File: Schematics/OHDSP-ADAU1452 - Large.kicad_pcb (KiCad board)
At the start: 2 copper layers, 100 x 100 mm, 305 parts, among them CN201 COAX, CN401 COAX, CN402 COAX, CN405 COAX, CN406 COAX, P201 CONN_2x1, P202 CONN_2x1, P203 CONN_6X2, P204 CONN_6x1, P301 CONN_2x1, P302 CONN_2x1, P303 PIN, P304 PIN, P305 PIN, P306 PIN, P601 CONN_02X05, P602 CONN_02X05, P603 CONN_02X05, P604 CONN_02X05, P605 CONN_3x1, P606 CONN_6X2, P607 CONN_02X05, P608 CONN_02X05, P609 CONN_02X20, P610 CONN_02X05, P611 CONN_5x1, P613 CONN_02X05, P614 CONN_02X05, P615 CONN_02X05, P616 CONN_02X05, SW201 SWITCH, SW202 SWITCH, U201 ADAU1452WBCPZ, U202 ADM13307-5ARZ, U203 25AA1024, U301 IC-REG-XRP7659ISTR-F, U302 IC-REG-XRP7659ISTR-F, U304 IC-REG-XC6210B332MR, U305 IC-REG-XC6210B332MR, U401 NB3L553, U501 IC-SPDIF-RX-OPTO, U502 IC-SPDIF-TX-OPTO, X201 24M576

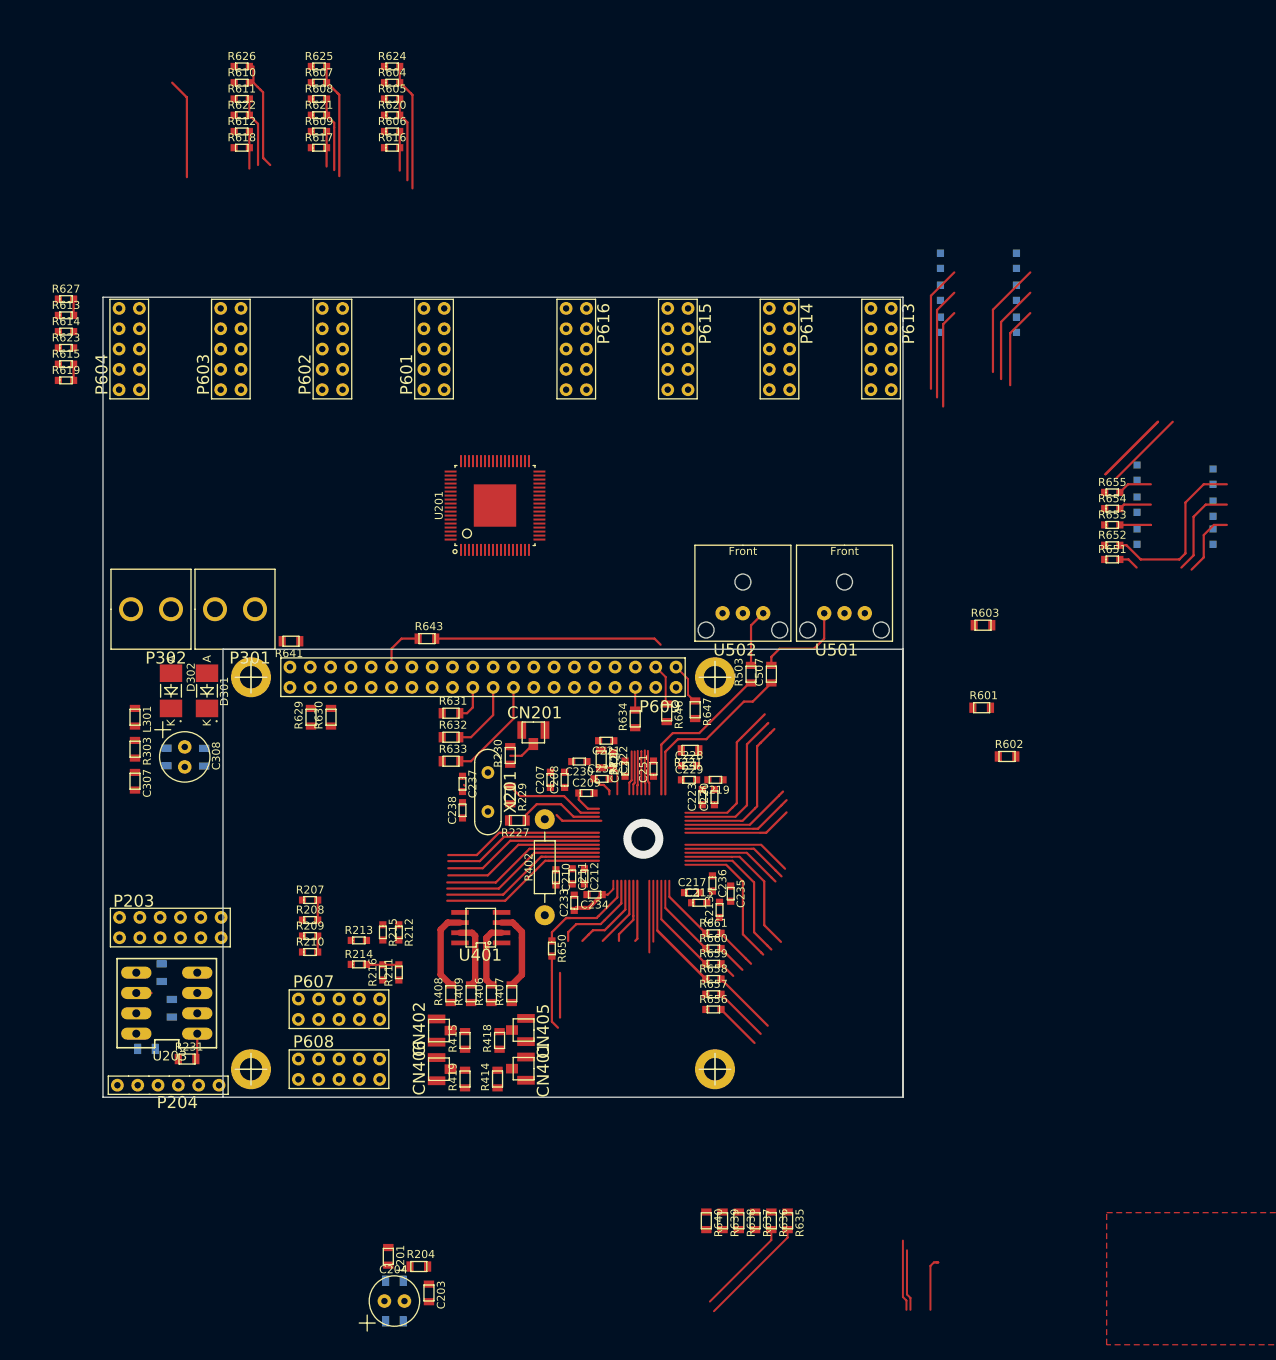
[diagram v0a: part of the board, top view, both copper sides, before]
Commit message: Add large pcb layout
Added large pcb layout, kicad created additional .pro file which can be
ignored, a bit of a hack but it works for the moment...
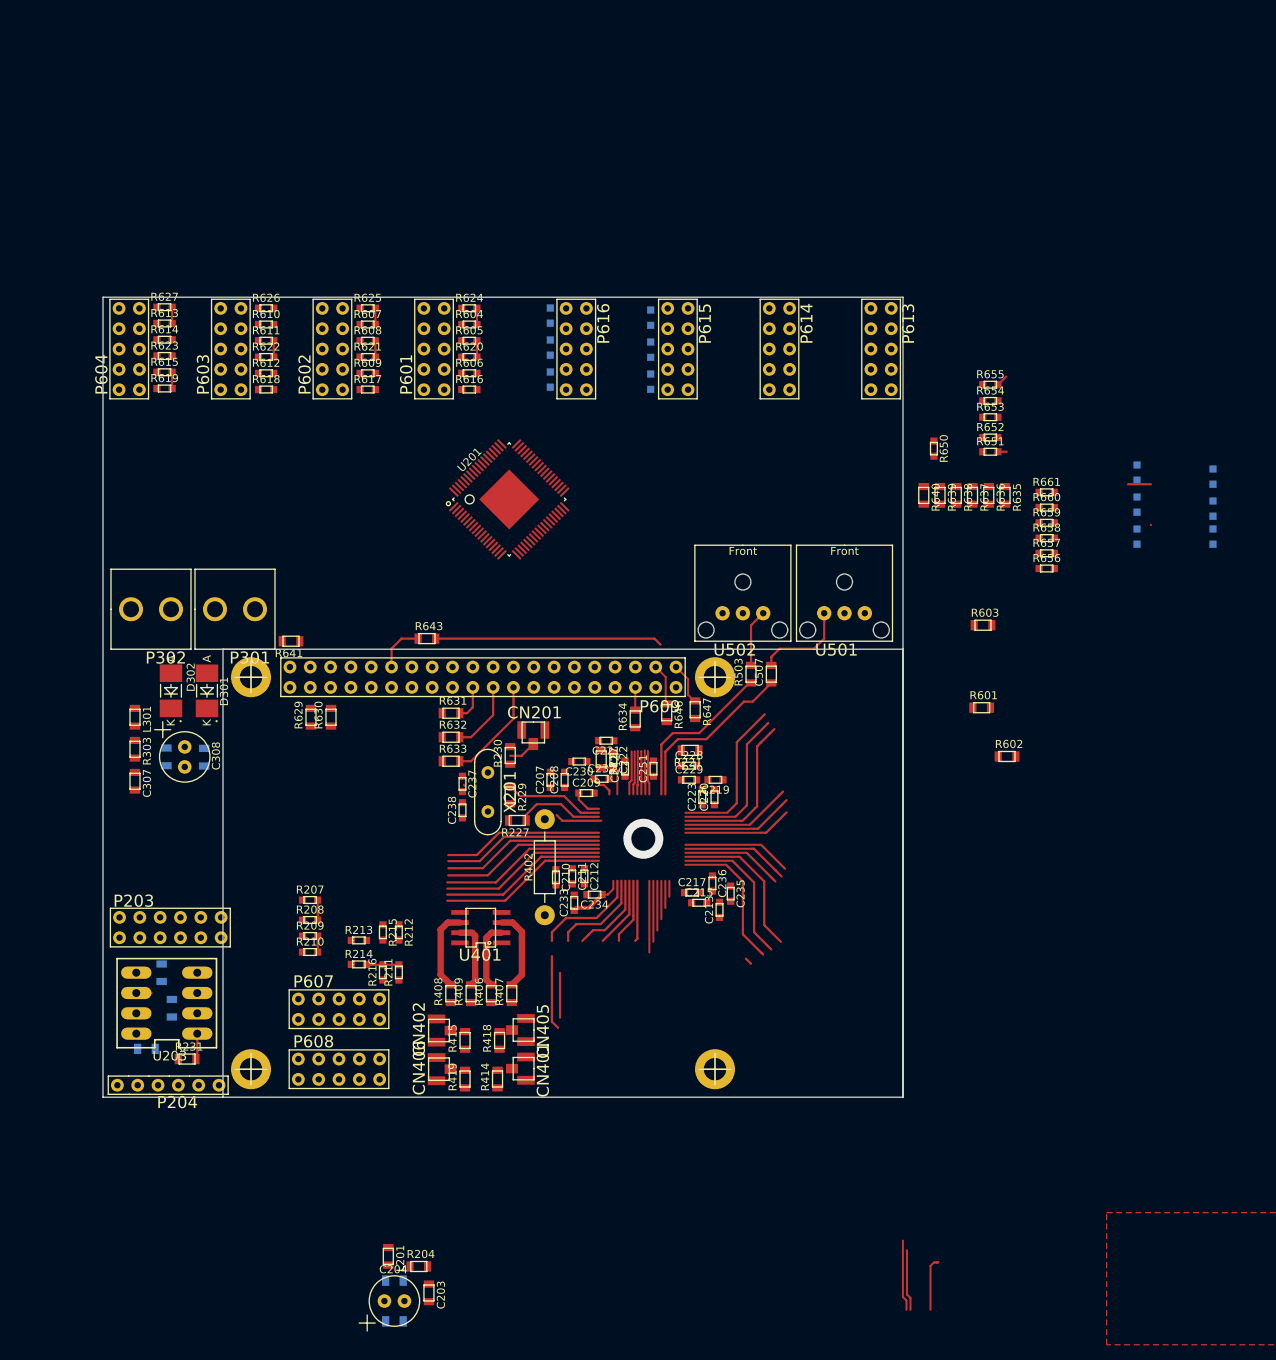
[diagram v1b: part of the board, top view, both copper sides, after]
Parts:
- moved R635 94.7 mm to (317.8, 48.8)
- moved R636 94.7 mm to (315.7, 48.8)
- moved R637 94.7 mm to (313.7, 48.8)
- moved R638 94.7 mm to (311.7, 48.8)
- moved R639 94.7 mm to (309.6, 48.8)
- moved R640 94.7 mm to (307.6, 48.8)
- moved R650 78.6 mm to (308.9, 42.9)
- moved R656 69.1 mm to (323.0, 57.9)
- moved R657 69.1 mm to (323.0, 56.0)
- moved R658 69.1 mm to (323.0, 54.1)
- moved R659 69.1 mm to (323.0, 52.2)
- moved R660 69.1 mm to (323.0, 50.3)
- moved R661 69.1 mm to (323.0, 48.4)
- moved R665 49.2 mm to (260.9, 26.3)
- moved R669 49.2 mm to (260.9, 30.3)
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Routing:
- net /ADAU1452/DACOUT_SDATA2: track 23.4 -> 0.00 mm
- net Net-(P615-Pad8): track 22.6 -> 0.00 mm
- net Net-(P613-Pad8): track 21.7 -> 0.00 mm
- net Net-(P616-Pad8): track 21.1 -> 0.06 mm
- net Net-(P615-Pad6): track 19.3 -> 0.00 mm
- net Net-(P616-Pad6): track 17.7 -> 0.00 mm
- net Net-(P613-Pad4): track 17.6 -> 0.00 mm
- net Net-(P615-Pad4): track 16.0 -> 0.00 mm
- net Net-(P616-Pad4): track 14.4 -> 0.00 mm
- net /Connectors/AUXADCIN_1: track 14.0 -> 0.00 mm
- net /ADAU1452/ADCIN_LRCLK0: track 15.9 -> 1.97 mm
- net /ADAU1452/DACOUT_LRCLK0: track 13.6 -> 0.00 mm
- net Net-(P613-Pad6): track 14.3 -> 1.08 mm
- net /ADAU1452/DACOUT_LRCLK3: track 12.7 -> 0.00 mm
- net /ADAU1452/ADCIN_LRCLK1: track 14.4 -> 2.10 mm
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
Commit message: Revert "Revert "Going 4 layer on smaller PCB""
This reverts commit a2928be1b12072271fc86fb10f3c648b88b658e1.
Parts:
- moved C252 152.7 mm to (359.0, 82.6), turned to 90 degrees
- moved P204 152.1 mm to (363.5, 73.5), turned to 270 degrees
- moved R231 150.6 mm to (360.2, 77.5), turned to 90 degrees
- moved R232 144.2 mm to (353.9, 79.4), turned to 180 degrees
- moved U203 143.9 mm to (353.2, 80.0), turned to 270 degrees
- moved C254 139.9 mm to (349.4, 80.6), turned to 180 degrees
- moved P203 133.0 mm to (344.4, 79.6), turned to 0 degrees
- moved U501 84.2 mm to (213.6, 58.2), turned to 180 degrees
- moved R414 83.5 mm to (302.5, 53.6), turned to 180 degrees
- moved CN406 83.4 mm to (303.3, 61.2), turned to 180 degrees
- moved R419 82.7 mm to (302.5, 57.7), turned to 180 degrees
- moved R602 80.2 mm to (244.1, 50.3), turned to 90 degrees
- moved CN401 79.9 mm to (299.2, 50.0), turned to 0 degrees
- moved R418 76.8 mm to (297.7, 53.4), turned to 180 degrees
- moved CN402 76.6 mm to (298.5, 61.2), turned to 180 degrees
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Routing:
- net (no net): track 537.1 -> 27.4 mm
- net /Connectors/RPI_BCLK: track 28.4 -> 0.00 mm
- net /ADAU1452/ADAU_SPDIF_RX: track 22.1 -> 0.00 mm
- net /ADAU1452/ADAU_SPDIF_TX: track 20.8 -> 0.00 mm
- net /ADAU1452/ADCIN_LRCLK0: track 1.97 -> 18.8 mm
- net /ADAU1452/DACOUT_LRCLK2: track 0.06 -> 14.4 mm
- net /ADAU1452/ADCIN_BCLK0: track 1.97 -> 14.7 mm
- net Net-(P616-Pad8): track 0.06 -> 12.6 mm
- net /ADAU1452/DACOUT_BCLK2: track 0.00 -> 12.5 mm
- net /ADAU1452/XTALIN: track 12.5 -> 0.00 mm
- net Net-(C507-Pad2): track 11.8 -> 0.00 mm
- net /ADAU1452/XTALOUT: track 11.0 -> 0.00 mm
- net /ADAU1452/ADCIN_SDATA0: track 0.00 -> 11.0 mm
- net /ADAU1452/DACOUT_SDATA2: track 0.00 -> 10.7 mm
- net Net-(P616-Pad6): track 0.00 -> 9.25 mm
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
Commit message: Revert "Going 4 layer on smaller PCB"
This reverts commit d1ec277a0becb058c7967dba94e28e7f31b1a00f.
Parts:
- moved C252 152.7 mm to (210.4, 118.0), turned to 0 degrees
- moved P204 152.1 mm to (219.5, 122.5), turned to 180 degrees
- moved R231 150.6 mm to (215.5, 119.2), turned to 0 degrees
- moved R232 144.2 mm to (213.6, 112.9), turned to 90 degrees
- moved U203 143.9 mm to (213.0, 112.2), turned to 180 degrees
- moved C254 139.9 mm to (212.3, 108.4), turned to 90 degrees
- moved P203 133.0 mm to (213.4, 102.8), turned to 270 degrees
- moved U501 84.2 mm to (297.7, 63.5), turned to 90 degrees
- moved R414 83.5 mm to (254.3, 121.7), turned to 90 degrees
- moved CN406 83.4 mm to (246.7, 122.5), turned to 90 degrees
- moved R419 82.7 mm to (250.3, 121.7), turned to 90 degrees
- moved R602 80.2 mm to (318.0, 81.4), turned to 0 degrees
- moved CN401 79.9 mm to (257.9, 118.4), turned to 270 degrees
- moved R418 76.8 mm to (254.6, 116.9), turned to 90 degrees
- moved CN402 76.6 mm to (246.7, 117.7), turned to 90 degrees
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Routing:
- net (no net): track 27.4 -> 537.1 mm
- net /Connectors/RPI_BCLK: track 0.00 -> 28.4 mm
- net /ADAU1452/ADAU_SPDIF_RX: track 0.00 -> 22.1 mm
- net /ADAU1452/ADAU_SPDIF_TX: track 0.00 -> 20.8 mm
- net /ADAU1452/ADCIN_LRCLK0: track 18.8 -> 1.97 mm
- net /ADAU1452/DACOUT_LRCLK2: track 14.4 -> 0.06 mm
- net /ADAU1452/ADCIN_BCLK0: track 14.7 -> 1.97 mm
- net Net-(P616-Pad8): track 12.6 -> 0.06 mm
- net /ADAU1452/DACOUT_BCLK2: track 12.5 -> 0.00 mm
- net /ADAU1452/XTALIN: track 0.00 -> 12.5 mm
- net Net-(C507-Pad2): track 0.00 -> 11.8 mm
- net /ADAU1452/XTALOUT: track 0.00 -> 11.0 mm
- net /ADAU1452/ADCIN_SDATA0: track 11.0 -> 0.00 mm
- net /ADAU1452/DACOUT_SDATA2: track 10.7 -> 0.00 mm
- net Net-(P616-Pad6): track 9.25 -> 0.00 mm
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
